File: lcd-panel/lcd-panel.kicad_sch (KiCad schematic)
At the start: 25 parts, among them J1 USB wire, J2 LCD FPC connector, J3 Fan Socket, Q1 AO3400A, U1 FT232H, U2 93LC56BT-I/OT, Y1 12.000 MHz

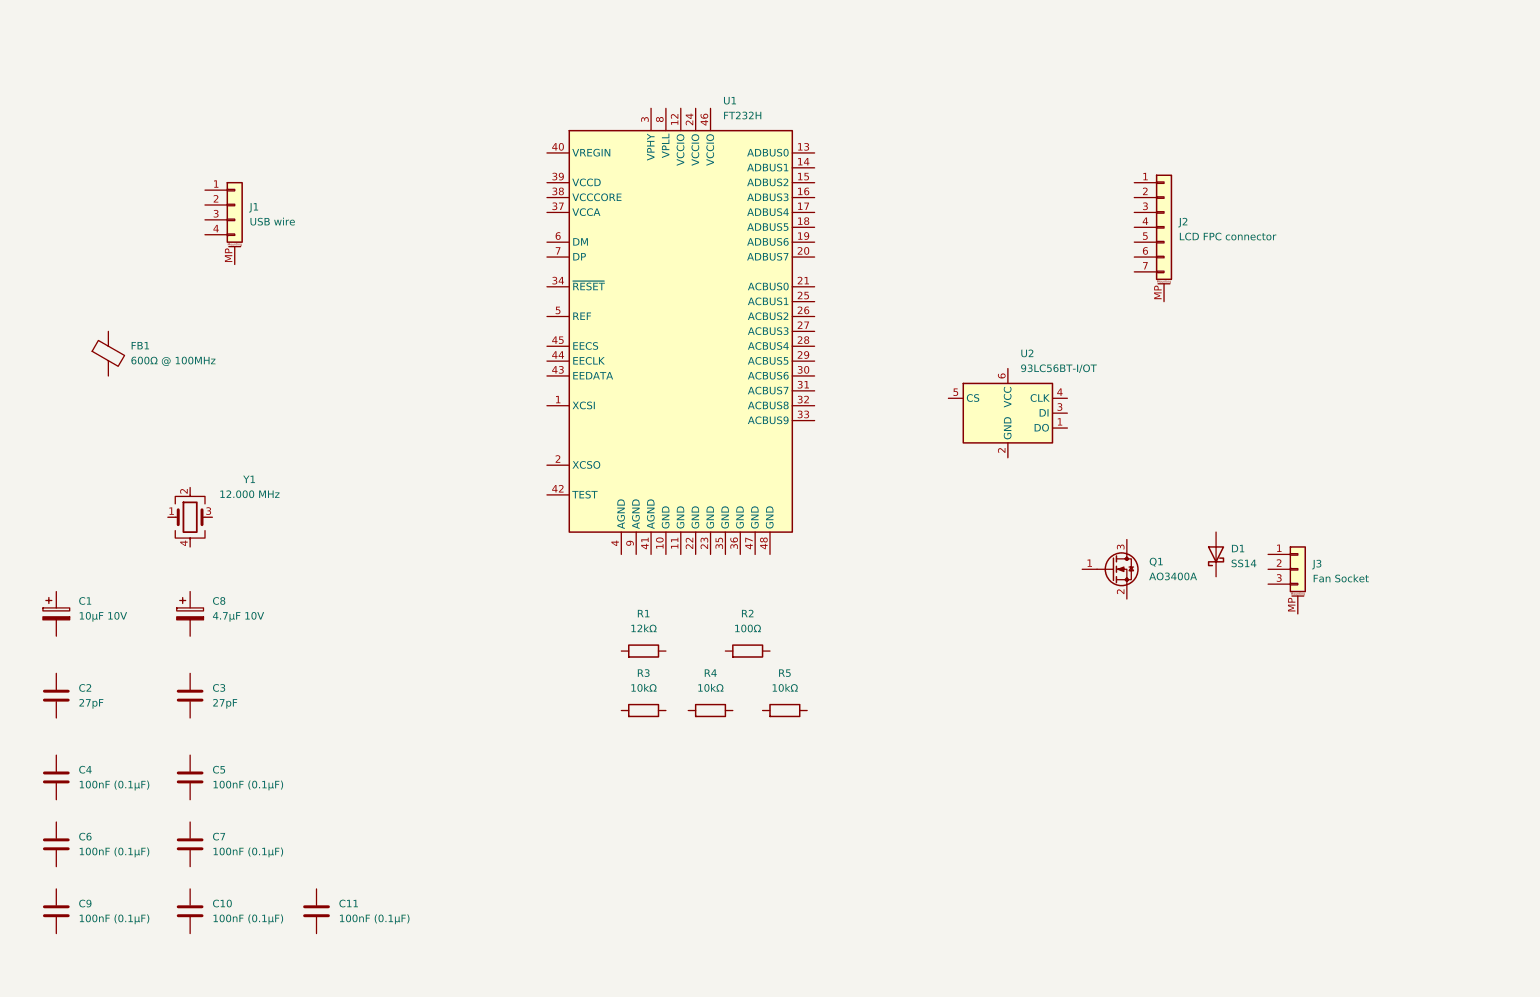
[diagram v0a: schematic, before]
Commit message: Adding the fan control wiring
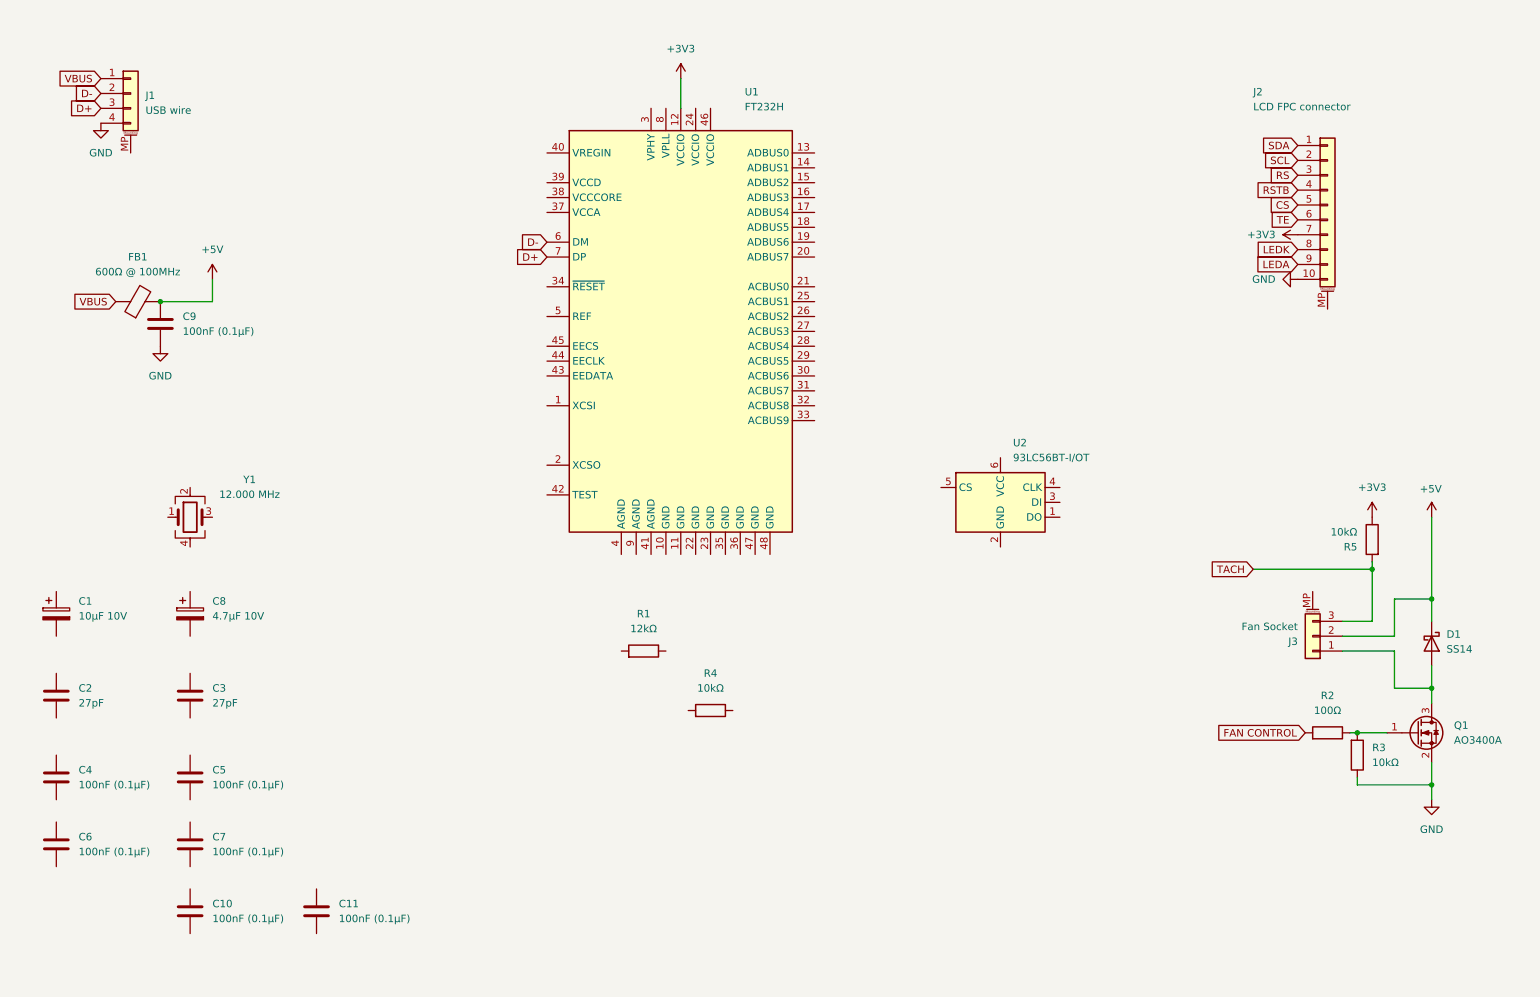
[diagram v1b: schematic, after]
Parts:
- J2: symbol Connector_Generic_MountingPin:Conn_01x07_MountingPin -> Connector_Generic_MountingPin:Conn_01x10_MountingPin
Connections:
- net +5V: now reaches D1.1 (K)
- net +5V: now also C9.1, FB1.2, J3.2 (Pin_2)
- net at D1.2 (A): now also J3.1 (Pin_1), Q1.3 (D)
- net GND: now reaches C9.2
- net GND: now also J1.4 (Pin_4), J2.10 (Pin_10), Q1.2 (S), R3.2
- net +3V3: now reaches U1.12 (VCCIO)
- net +3V3: now also J2.7 (Pin_7), R5.2
- net D-: now reaches U1.6 (DM)
- net D-: now also J1.2 (Pin_2)
- net D+: now reaches U1.7 (DP)
- net D+: now also J1.3 (Pin_3)
- net SDA: now reaches J2.1 (Pin_1)
- net SCL: now reaches J2.2 (Pin_2)
- net RS: now reaches J2.3 (Pin_3)
- net RSTB: now reaches J2.4 (Pin_4)
- net CS: now reaches J2.5 (Pin_5)
- net TE: now reaches J2.6 (Pin_6)
- net TACH: now reaches J3.3 (Pin_3)
- net TACH: now also R5.1
- net at Q1.1 (G): now also R2.2, R3.1
- net FAN CONTROL: now reaches R2.1
- net VBUS: now reaches J1.1 (Pin_1)
- net VBUS: now also FB1.1
- new net LEDA: J2.9 (Pin_9)
- new net LEDK: J2.8 (Pin_8)
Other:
- moved on the sheet: C9, D1, FB1, J1, J3, Q1, R2, R3, R5, U2

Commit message: Adding the baseline LCD wiring
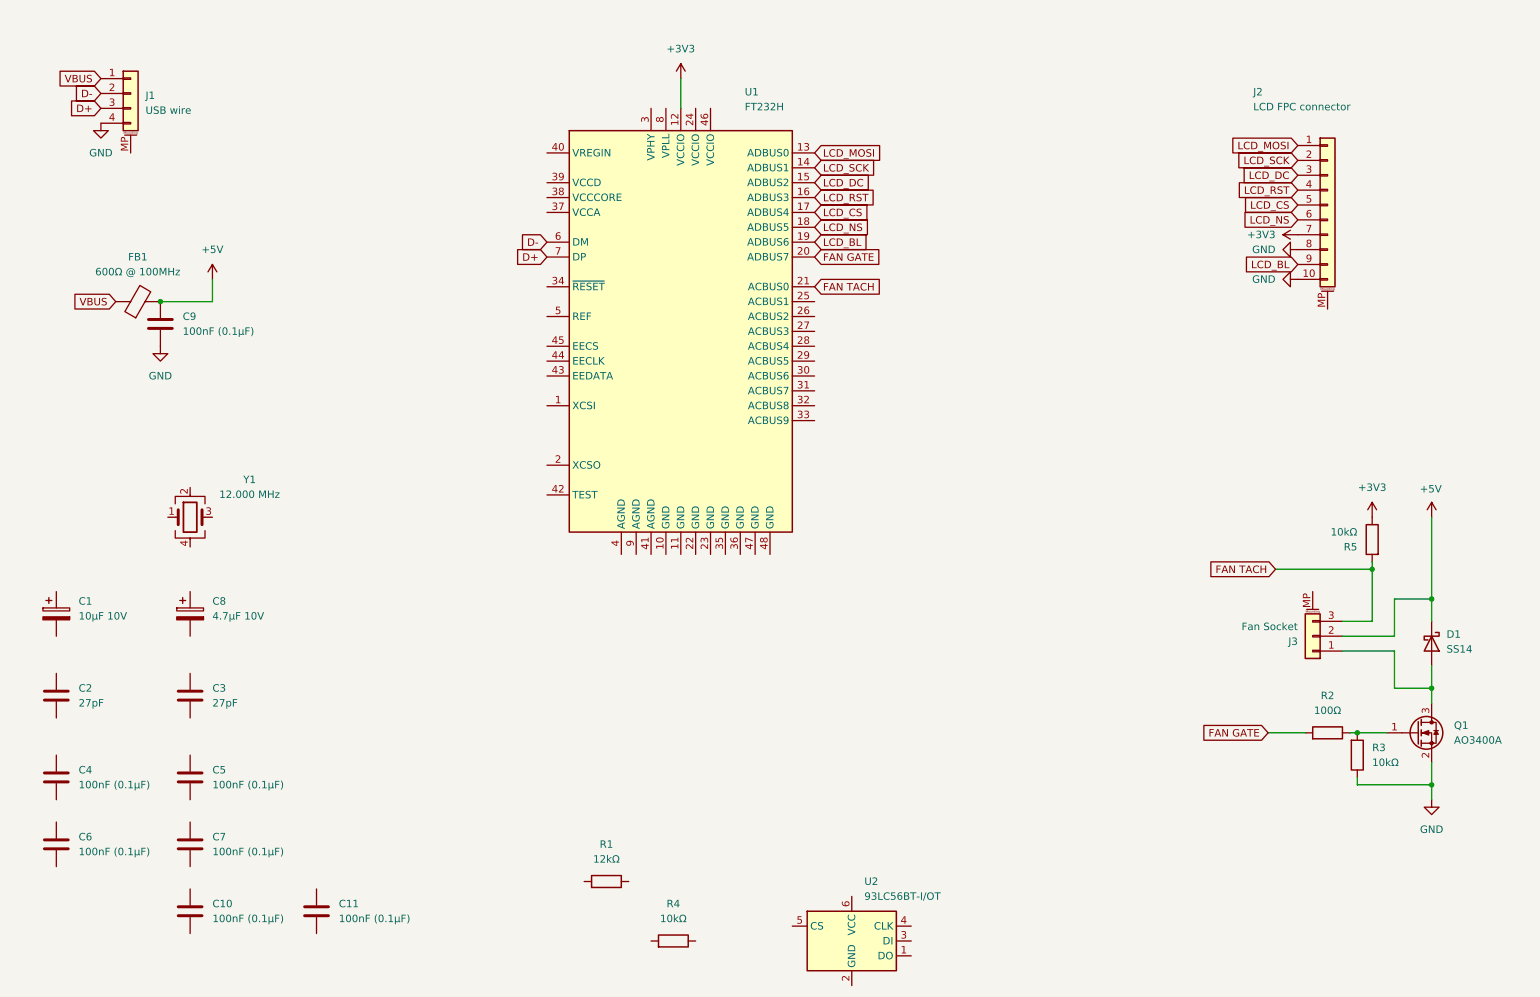
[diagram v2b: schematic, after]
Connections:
- net CS is gone; now on net LCD_CS: J2.5 (Pin_5)
- net FAN CONTROL is gone; now on net FAN GATE: R2.1
- net LEDA is gone; now on net LCD_BL: J2.9 (Pin_9)
- net LEDK is gone; now on net GND: J2.8 (Pin_8)
- net RS is gone; now on net LCD_DC: J2.3 (Pin_3)
- net RSTB is gone; now on net LCD_RST: J2.4 (Pin_4)
- net SCL is gone; now on net LCD_SCK: J2.2 (Pin_2)
- net SDA is gone; now on net LCD_MOSI: J2.1 (Pin_1)
- net TACH is gone; now on net FAN TACH: J3.3 (Pin_3), R5.1
- net TE is gone; now on net LCD_NS: J2.6 (Pin_6)
- net LCD_MOSI: now reaches U1.13 (ADBUS0)
- net LCD_SCK: now reaches U1.14 (ADBUS1)
- net LCD_DC: now reaches U1.15 (ADBUS2)
- net LCD_RST: now reaches U1.16 (ADBUS3)
- net LCD_CS: now reaches U1.17 (ADBUS4)
- net LCD_NS: now reaches U1.18 (ADBUS5)
- net LCD_BL: now reaches U1.19 (ADBUS6)
- net FAN GATE: now reaches U1.20 (ADBUS7)
- net FAN TACH: now reaches U1.21 (ACBUS0)
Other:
- moved on the sheet: R1, R4, U2

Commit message: Brushing up BOM an sorting out power wiring
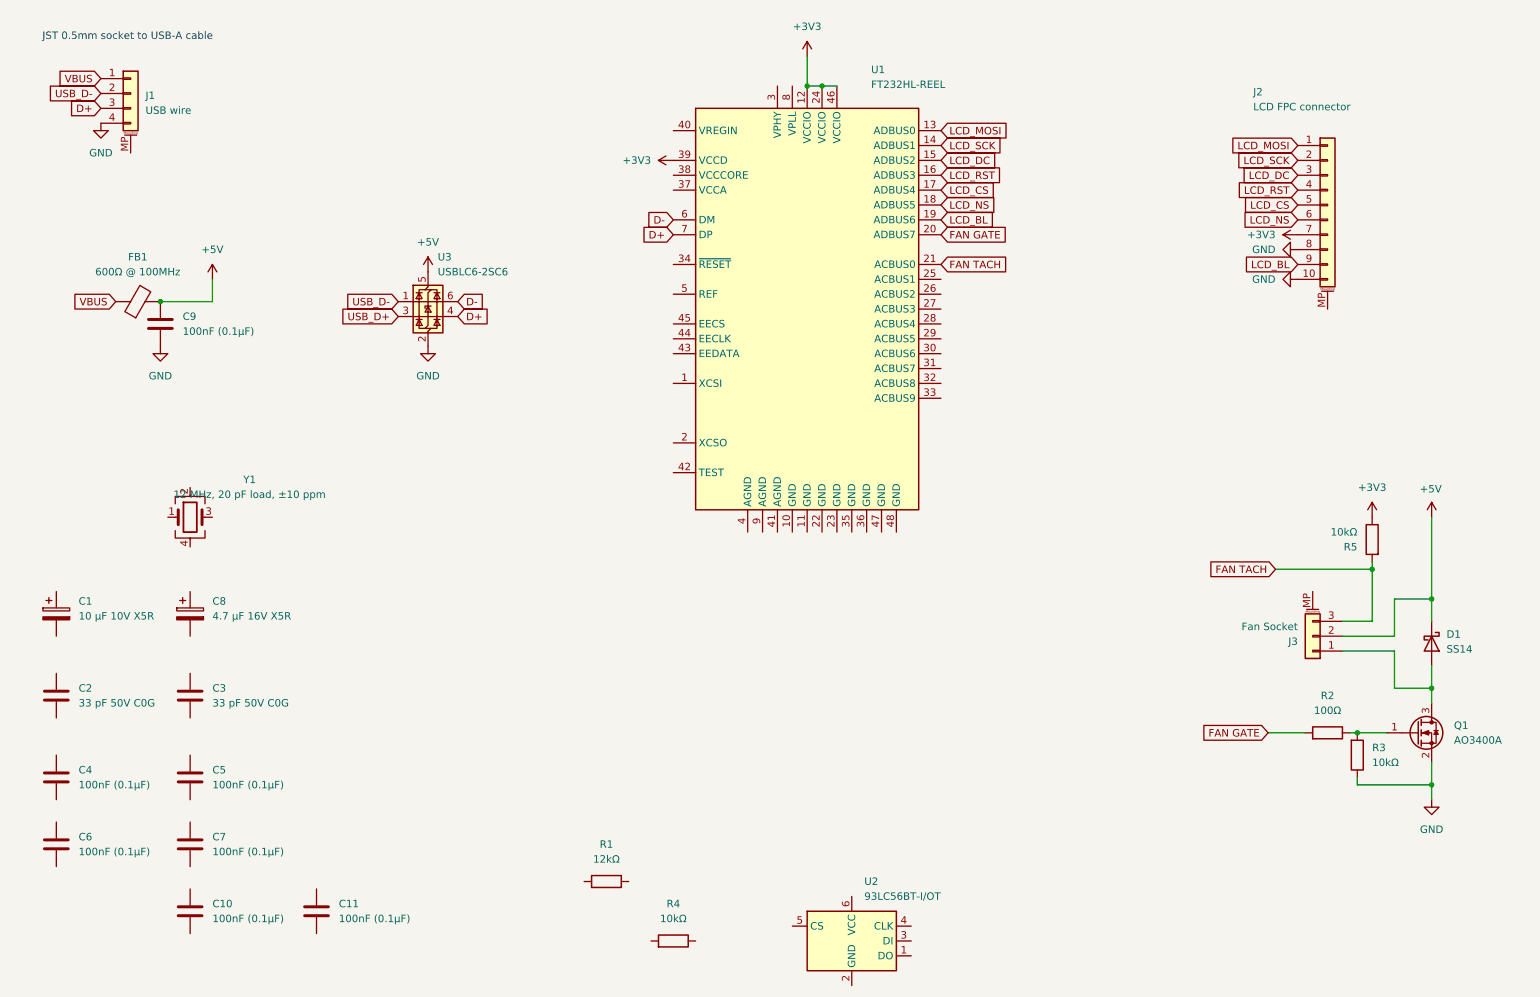
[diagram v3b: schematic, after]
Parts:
- added U3: USBLC6-2SC6, Package_TO_SOT_SMD:SOT-23-6, symbol Power_Protection:USBLC6-2SC6
- C1: value 10µF 10V -> 10 µF 10V X5R
- C2, C3: value 27pF -> 33 pF 50V C0G; LCSC C1524 -> C1562
- C8: value 4.7µF 10V -> 4.7 µF 16V X5R
- D1: LCSC C2474 -> C2480
- FB1: LCSC C1015 -> C96708
- R1: LCSC C25782 -> C25752
- U1: value FT232H -> FT232HL-REEL; footprint Package_DFN_QFN:QFN-48-1EP_7x7mm_P0.5mm_EP5.15x5.15mm -> Package_QFP:LQFP-48_7x7mm_P0.5mm; LCSC C14953 -> C51997
- Y1: value 12.000 MHz -> 12 MHz, 20 pF load, ±10 ppm; LCSC C13738 -> C9002
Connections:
- net +3V3: now also U1.24 (VCCIO), U1.39 (VCCD), U1.46 (VCCIO)
- net +5V: now also U3.5 (VBUS)
- net D+: now also U3.4 (I/O2)
- net D-: now also U3.6 (I/O1); no longer J1.2 (Pin_2)
- net GND: now also U3.2 (GND)
- new net USB_D+: U3.3 (I/O2)
- new net USB_D-: J1.2 (Pin_2), U3.1 (I/O1)
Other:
- note added: "JST 0.5mm socket to USB-A cable"
- moved on the sheet: U1

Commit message: Wiring the EEPROM
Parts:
- added R5: 2.2kΩ, Resistor_SMD:R_0402_1005Metric, symbol PCM_Resistor_AKL:R_0603
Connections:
- net +3V3: now also U2.6 (VCC)
- net +5V: now also U1.40 (VREGIN)
- net GND: now also U2.2 (GND)
- net EEDATA: now reaches U1.43 (EEDATA)
- net EEDATA: now also U2.3 (DI), R5.2
- net EECLK: now reaches U1.44 (EECLK)
- net EECLK: now also U2.4 (CLK)
- net EECS: now reaches U1.45 (EECS)
- net EECS: now also U2.5 (CS)
- net at U2.1 (DO): now also R5.1
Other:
- moved on the sheet: U1, U2
